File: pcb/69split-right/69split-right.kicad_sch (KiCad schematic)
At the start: 0 parts

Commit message: Figured out what GPIOs to use.
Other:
- note added: "69SPLIT RIGHT KEYBOARD"
- note added: "GPIO Outputs"
- note added: "Keyboard USB-C Connection"
- note added: "Left Keyboard"
- note added: "USB-C to PC"
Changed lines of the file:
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@@
 	(generator_version "9.0")
 	(paper "A4")
+	(arc
+		(start 103.505 97.79)
+		(mid 141.605 60.3602)
+		(end 179.705 97.79)
+		(stroke
+			(width 0)
+			(type solid)
+			(color 0 0 0 1)
+		)
+		(fill
+			(type none)
+		)
+	)
+	(rectangle
+		(start 78.74 97.79)
+		(end 130.175 152.4)
+		(stroke
+			(width 0)
+			(type default)
+		)
+		(fill
+			(type none)
+		)
+	)
+	(text "69SPLIT RIGHT KEYBOARD"
+		(exclude_from_sim no)
+		(at 143.51 36.576 0)
+		(effects
+			(font
+				(face "Book Antiqua")
+				(size 7.62 7.62)
+				(color 0 0 0 1)
+			)
+		)
+	)
+	(text "GPIO Outputs"
+		(exclude_from_sim no)
+		(at 200.025 72.644 0)
+		(effects
+			(font
+				(size 1.27 1.27)
+				(color 0 0 0 1)
+			)
+			(justify left)
+		)
+	)
+	(text "Keyboard USB-C Connection"
+		(exclude_from_sim no)
+		(at 127.635 67.31 0)
+		(effects
+			(font
+				(size 1.27 1.27)
+				(color 0 0 0 1)
+			)
+			(justify left)
+		)
+	)
+	(text "USB-C to PC"
+		(exclude_from_sim no)
+		(at 81.915 72.39 0)
+		(effects
+			(font
+				(size 1.27 1.27)
+				(color 0 0 0 1)
+			)
+			(justify left)
+		)
+	)
+	(text "Left Keyboard"
+		(exclude_from_sim no)
+		(at 102.87 123.444 0)
+		(effects
+			(font
+				(size 1.27 1.27)
+			)
+		)
+	)
+	(polyline
+		(pts
+			(xy 206.375 74.93) (xy 206.375 97.79)
+		)
+		(stroke
+			(width 0)
+			(type default)
+			(color 0 0 0 1)
+		)
+	)
+	(polyline
+		(pts
+			(xy 89.535 74.93) (xy 89.535 97.79)
+		)
+		(stroke
+			(width 0)
+			(type default)
+			(color 0 0 0 1)
+		)
+	)
+	(polyline
+		(pts
+			(xy 201.295 74.93) (xy 201.295 97.79)
+		)
+		(stroke
+			(width 0)
+			(type default)
+			(color 0 0 0 1)
+		)
+	)
+	(polyline
+		(pts
+			(xy 211.455 74.93) (xy 211.455 97.79)
+		)
+		(stroke
+			(width 0)
+			(type default)
+			(color 0 0 0 1)
+		)
+	)
+	(polyline
+		(pts
+			(xy 84.455 74.93) (xy 84.455 97.79)
+		)
+		(stroke
+			(width 0)
+			(type default)
+			(color 0 0 0 1)
+		)
+	)
 	(sheet
-		(at 111.76 72.39)
-		(size 41.91 54.61)
+		(at 156.21 97.79)
+		(size 58.42 54.61)
 		(exclude_from_sim no)
 		(in_bom yes)
@@
 		)
 		(property "Sheetname" "69split Right Keyboard"
-			(at 111.76 71.6784 0)
+			(at 156.21 97.0784 0)
 			(effects
 				(font
@@
 		)
 		(property "Sheetfile" "../right.kicad_sch"
-			(at 111.76 127.5846 0)
+			(at 156.21 152.9846 0)
 			(effects
 				(font

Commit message: I think schematic is done?
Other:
- title: (none) -> 69SPLIT KEYBOARD
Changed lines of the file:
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@@
 	(generator_version "9.0")
 	(paper "A4")
+	(title_block
+		(title "69SPLIT KEYBOARD")
+		(date "2025-06-11")
+	)
 	(arc
 		(start 103.505 97.79)

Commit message: Moved things around so it's less confusing.
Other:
- removed sheet 69split Right Keyboard
- added sheet GPIO Outputs (gpio.kicad_sch)
- added sheet Right Keyboard Connector (right-conn.kicad_sch)
- added sheet Right Matrix (right-matrix.kicad_sch)
- note added: "69SPLIT KEYBOARD"
- note added: "RIGHT SIDE"
- note removed: "69SPLIT RIGHT KEYBOARD"

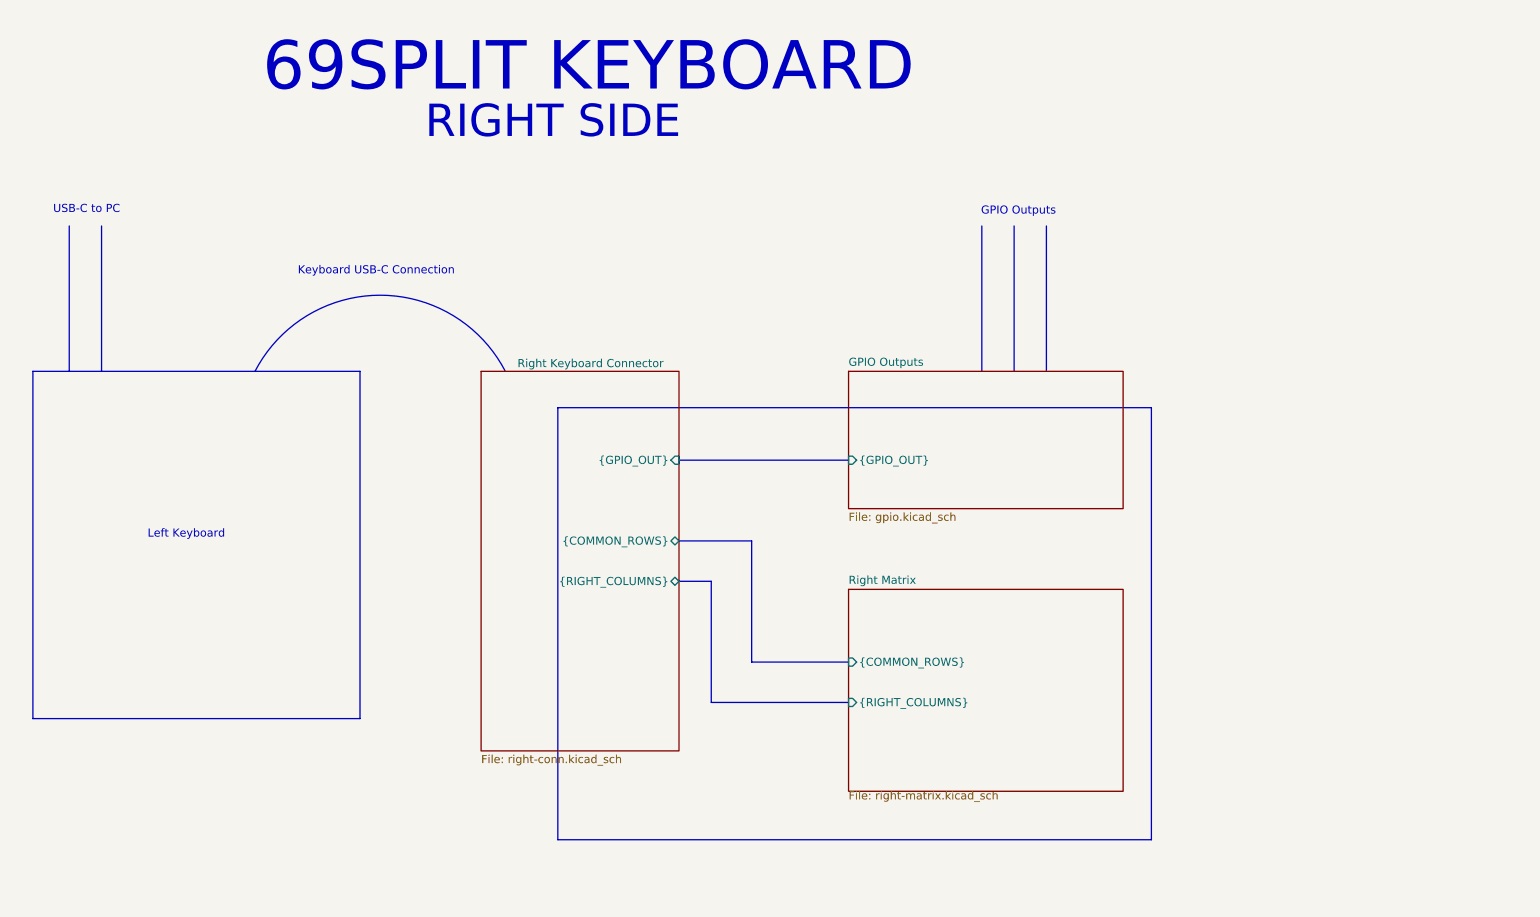
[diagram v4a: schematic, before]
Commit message: Started changing things gain to use an I/O expander with I2C.
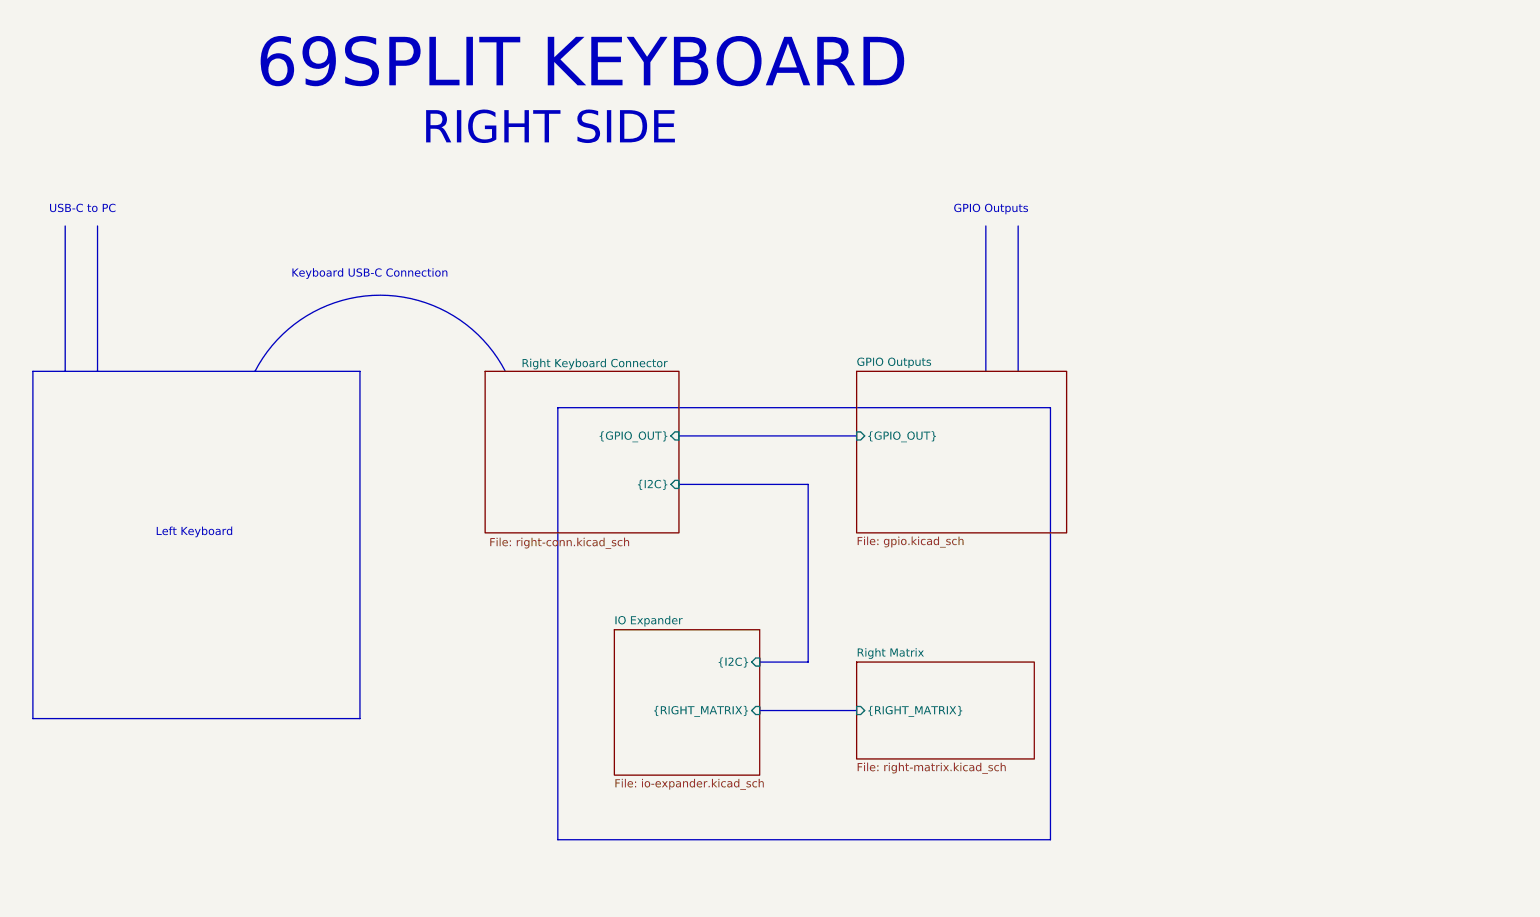
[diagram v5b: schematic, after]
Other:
- added sheet IO Expander (io-expander.kicad_sch)
- sheet Right Keyboard Connector ports: added {I2C}; removed {COMMON_ROWS}, {RIGHT_COLUMNS}
- sheet Right Matrix ports: added {RIGHT_MATRIX}; removed {COMMON_ROWS}, {RIGHT_COLUMNS}
- title: 69SPLIT KEYBOARD -> 69SPLIT
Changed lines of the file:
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@@
 	(paper "A4")
 	(title_block
-		(title "69SPLIT KEYBOARD")
-		(date "2025-06-11")
+		(title "69SPLIT")
+		(date "2025-07-28")
 		(rev "1")
 		(comment 1 "Yiannis Michael")
@@
 	(rectangle
 		(start 143.51 81.915)
-		(end 236.855 149.86)
+		(end 220.98 149.86)
 		(stroke
 			(width 0)
@@
 	(text "GPIO Outputs"
 		(exclude_from_sim no)
-		(at 210.058 51.054 0)
+		(at 205.74 50.8 0)
 		(effects
 			(font
@@
 	(text "RIGHT SIDE"
 		(exclude_from_sim no)
-		(at 142.748 37.084 0)
+		(at 142.24 38.1 0)
 		(effects
 			(font
@@
 	(text "Keyboard USB-C Connection"
 		(exclude_from_sim no)
-		(at 102.616 60.452 0)
+		(at 101.6 60.96 0)
 		(effects
 			(font
@@
 	(text "USB-C to PC"
 		(exclude_from_sim no)
-		(at 64.135 50.8 0)
+		(at 63.5 50.8 0)
 		(effects
 			(font
@@
 	(text "69SPLIT KEYBOARD"
 		(exclude_from_sim no)
-		(at 148.336 28.448 0)
+		(at 147.32 27.94 0)
 		(effects
 			(font
@@
 	(text "Left Keyboard"
 		(exclude_from_sim no)
-		(at 85.09 101.854 0)
+		(at 86.36 101.6 0)
 		(effects
 			(font
@@
 	(bus
 		(pts
-			(xy 173.99 121.92) (xy 173.99 102.87)
+			(xy 182.88 121.92) (xy 182.88 93.98)
 		)
 		(stroke
@@
 	(polyline
 		(pts
-			(xy 215.265 53.34) (xy 215.265 76.2)
+			(xy 215.9 53.34) (xy 215.9 76.2)
 		)
 		(stroke
@@
 		)
 	)
+	(polyline
+		(pts
+			(xy 71.12 53.34) (xy 71.12 76.2)
+		)
+		(stroke
+			(width 0)
+			(type default)
+			(color 0 0 0 1)
+		)
+	)
+	(polyline
+		(pts
+			(xy 210.82 53.34) (xy 210.82 76.2)
+		)
+		(stroke
+			(width 0)
+			(type default)
+			(color 0 0 0 1)
+		)
+	)
 	(bus
 		(pts
-			(xy 167.64 109.22) (xy 162.56 109.22)
+			(xy 182.88 93.98) (xy 162.56 93.98)
+		)
+		(stroke
+			(width 0)
+			(type default)
+		)
+	)
+	(bus
+		(pts
+			(xy 175.26 129.54) (xy 190.5 129.54)
+		)
+		(stroke
+			(width 0)
+			(type default)
+		)
+	)
+	(bus
+		(pts
+			(xy 162.56 86.36) (xy 190.5 86.36)
 		)
 		(stroke
@@
 	(polyline
 		(pts
-			(xy 71.755 53.34) (xy 71.755 76.2)
+			(xy 66.04 53.34) (xy 66.04 76.2)
 		)
 		(stroke
@@
 		)
 	)
-	(polyline
-		(pts
-			(xy 210.185 53.34) (xy 210.185 76.2)
-		)
-		(stroke
-			(width 0)
-			(type default)
-			(color 0 0 0 1)
-		)
-	)
 	(bus
 		(pts
-			(xy 167.64 128.27) (xy 167.64 109.22)
-		)
-		(stroke
-			(width 0)
-			(type default)
-		)
-	)
-	(polyline
-		(pts
-			(xy 220.345 53.34) (xy 220.345 76.2)
-		)
-		(stroke
-			(width 0)
-			(type default)
-			(color 0 0 0 1)
-		)
-	)
-	(bus
-		(pts
-			(xy 173.99 102.87) (xy 162.56 102.87)
-		)
-		(stroke
-			(width 0)
-			(type default)
-		)
-	)
-	(bus
-		(pts
-			(xy 167.64 128.27) (xy 189.23 128.27)
-		)
-		(stroke
-			(width 0)
-			(type default)
-		)
-	)
-	(bus
-		(pts
-			(xy 173.99 121.92) (xy 189.23 121.92)
-		)
-		(stroke
-			(width 0)
-			(type default)
-		)
-	)
-	(bus
-		(pts
-			(xy 162.56 90.17) (xy 189.23 90.17)
-		)
-		(stroke
-			(width 0)
-			(type default)
-		)
-	)
-	(polyline
-		(pts
-			(xy 66.675 53.34) (xy 66.675 76.2)
-		)
-		(stroke
-			(width 0)
-			(type default)
-			(color 0 0 0 1)
+			(xy 175.26 121.92) (xy 182.88 121.92)
+		)
+		(stroke
+			(width 0)
+			(type default)
 		)
 	)
 	(sheet
-		(at 189.23 110.49)
-		(size 43.18 31.75)
+		(at 190.5 121.92)
+		(size 27.94 15.24)
 		(exclude_from_sim no)
 		(in_bom yes)
@@
 		)
 		(property "Sheetname" "Right Matrix"
-			(at 189.23 109.7784 0)
+			(at 190.5 121.2084 0)
 			(effects
 				(font
@@
 		)
 		(property "Sheetfile" "right-matrix.kicad_sch"
-			(at 189.23 142.1896 0)
+			(at 190.5 137.7446 0)
 			(effects
 				(font
@@
 			)
 		)
-		(pin "{COMMON_ROWS}" input
-			(at 189.23 121.92 180)
-			(effects
-				(font
-					(size 1.27 1.27)
-				)
-				(justify left)
-			)
-		)
-		(pin "{RIGHT_COLUMNS}" input
-			(at 189.23 128.27 180)
+		(pin "{RIGHT_MATRIX}" input
+			(at 190.5 129.54 180)
 			(effects
 				(font
@@
 				)
 			)
+			(project ""
+				(path "/525264c0-2406-4b67-890e-0f0fc62e1056"
+					(page "#")
+				)
+			)
+			(project "69split"
+				(path "/1573ac28-80e2-4ab2-b20c-1c4896f37ece/525264c0-2406-4b67-890e-0f0fc62e1056"
+					(page "11")
+				)
+			)
 		)
 	)
 	(sheet
-		(at 131.445 76.2)
-		(size 31.115 59.69)
+		(at 152.4 116.84)
+		(size 22.86 22.86)
 		(exclude_from_sim no)
 		(in_bom yes)
 		(on_board yes)
 		(dnp no)
+		(fields_autoplaced yes)
 		(stroke
 			(width 0.1524)
@@
 			(color 0 0 0 0.0000)
 		)
+		(property "Sheetname" "IO Expander"
+			(at 152.4 116.1284 0)
+			(effects
+				(font
+					(size 1.27 1.27)
+				)
+				(justify left bottom)
+			)
+		)
+		(property "Sheetfile" "io-expander.kicad_sch"
+			(at 152.4 140.2846 0)
+			(effects
+				(font
+					(size 1.27 1.27)
+				)
+				(justify left top)
+			)
+		)
+		(pin "{I2C}" input
+			(at 175.26 121.92 0)
+			(effects
+				(font
+					(size 1.27 1.27)
+				)
+				(justify right)
+			)
+		)
+		(pin "{RIGHT_MATRIX}" input
+			(at 175.26 129.54 0)
+			(effects
+				(font
+					(size 1.27 1.27)
+				)
+				(justify right)
+			)
+		)
+		(instances
+			(project "69split-right"
+				(path "/f79c3bfa-40a7-4d04-ac4b-e56fce3d0867"
+					(page "5")
+				)
+			)
+		)
+	)
+	(sheet
+		(at 132.08 76.2)
+		(size 30.48 25.4)
+		(exclude_from_sim no)
+		(in_bom yes)
+		(on_board yes)
+		(dnp no)
+		(stroke
+			(width 0.1524)
+			(type solid)
+		)
+		(fill
+			(color 0 0 0 0.0000)
+		)
 		(property "Sheetname" "Right Keyboard Connector"
-			(at 137.16 75.692 0)
+			(at 137.795 75.692 0)
 			(effects
 				(font
@@
 		)
 		(property "Sheetfile" "right-conn.kicad_sch"
-			(at 131.445 136.4746 0)
+			(at 132.715 102.362 0)
 			(effects
 				(font
@@
 			)
 		)
-		(pin "{COMMON_ROWS}" bidirectional
-			(at 162.56 102.87 0)
+		(pin "{GPIO_OUT}" input
+			(at 162.56 86.36 0)
 			(effects
 				(font
@@
 			)
 		)
-		(pin "{RIGHT_COLUMNS}" bidirectional
-			(at 162.56 109.22 0)
-			(effects
-				(font
-					(size 1.27 1.27)
-					(thickness 0.1588)
-				)
-				(justify right)
-			)
-		)
-		(pin "{GPIO_OUT}" input
-			(at 162.56 90.17 0)
+		(pin "{I2C}" input
+			(at 162.56 93.98 0)
 			(effects
 				(font
@@
 				)
 			)
+			(project ""
+				(path "/525264c0-2406-4b67-890e-0f0fc62e1056"
+					(page "#")
+				)
+			)
+			(project "69split"
+				(path "/1573ac28-80e2-4ab2-b20c-1c4896f37ece/525264c0-2406-4b67-890e-0f0fc62e1056"
+					(page "9")
+				)
+			)
 		)
 	)
 	(sheet
-		(at 189.23 76.2)
-		(size 43.18 21.59)
+		(at 190.5 76.2)
+		(size 33.02 25.4)
 		(exclude_from_sim no)
 		(in_bom yes)
@@
 		)
 		(property "Sheetname" "GPIO Outputs"
-			(at 189.23 75.4884 0)
+			(at 190.5 75.4884 0)
 			(effects
 				(font
@@
 		)
 		(property "Sheetfile" "gpio.kicad_sch"
-			(at 189.23 98.3746 0)
+			(at 190.5 102.1846 0)
 			(effects
 				(font
@@
 		)
 		(pin "{GPIO_OUT}" input
-			(at 189.23 90.17 180)
+			(at 190.5 86.36 180)
 			(effects
 				(font
@@
 				)
 			)
-		)
-	)
-	(sheet_instances
-		(path "/"
-			(page "1")
-		)
-	)
-	(embedded_fonts no)
-	(embedded_files
-		(file
-			(name "my-sheet.kicad_wks")
-			(type worksheet)
-			(data |KLUv/WCfCS0VANadXiEQ0zb8P046AJ8aXgsH2O6IQXYrqPActbgvTGkjAgg3cCBVAFEAWAB7LP/L
-				zyw/g9G7Wic1Zntj95csGrCl1TMfak8mtWjA1HoO6fM/+QsAQEBgcj6flV5SJ+kwd6Ip+S7f25nM
-				GINlrZ1uvU6W+ty5UwAEBOfG04UeqDeFmyYieCK/t9h7g3Z+MoMOuug/ORp83WKgi71+31ftVAA8
-				WV6s4+tnaUpW8v/k/x7XCV+vGPTZIKmvv5fN7NVDMu9M7hJ8sfpv709J8jx65IM514baP+fMNtk7
-				OIwGoSb5e+MuL76z6U0o2QSbhPQWiuXnFKVZMkonUyxL8tADtUPyJ/M4lqCllL0iEm2jZJZugSk0
-				h4iAKab4XrVeFOEITC/EKOOwRZdVtgGB4bqUou7OZ4UirF9WRavlIhkEIlGAPic93r72wtU1YXvp
-				pShb6XVcXYu6cFVVWjU4bMJlWWOzrIlSECySPTSGZoBa9F674fqtaLXZg9M48TV3bYCCoOFA5pgZ
-				GklBmgxjgESExqwbzSlGCpJs4MLuYpN32QM4R7fcqQEYZYbBFb1roCZzALF1NlkveCyCWL35cxnE
-				wEKI4KJj0KsXBr6oiI1J+MtQQe+wUhcnvps4Rq/BHcNqTNlOEzNBhptObKt4AIWcYgJSlH9RNGOF
-				4k2HgwPJg0yfmc/CAzU75BLHuyCsTniNFbERpgVEeEgINsEyhIZBhCUXYQhCwScM5iHza+yObgD2
-				rqfvQX3GtNTki66yMw857Cm3qOsujTSVhoEY/SH9Q5Ui707wgLy7+D2sP38Sbw3rjn/tfXLTei5t
-				wgDnVU9KDVYzrAHGAIE4CQf8nZQ1Aw8ByJ0t3qRoW1pWI4TomR9hr1HcpCVt2Lj0DctF1FRG+kCN
-				Qa8C|
-			)
-			(checksum "4C3981DD706FE33EF3AD57A4258970D5")
-		)
-	)
+			(project ""
+				(path "/525264c0-2406-4b67-890e-0f0fc62e1056"
+					(page "#")
+				)
+			)
+			(project "69split"
+				(path "/1573ac28-80e2-4ab2-b20c-1c4896f37ece/525264c0-2406-4b67-890e-0f0fc62e1056"
+					(page "10")
+				)
+			)
+		)
+	)

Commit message: Alright I think now the left side is actually ready.
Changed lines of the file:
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@@
 	(bus
 		(pts
-			(xy 182.88 121.92) (xy 182.88 93.98)
+			(xy 180.34 121.92) (xy 180.34 93.98)
 		)
 		(stroke
@@
 	(bus
 		(pts
-			(xy 182.88 93.98) (xy 162.56 93.98)
+			(xy 180.34 93.98) (xy 162.56 93.98)
 		)
 		(stroke
@@
 	(bus
 		(pts
-			(xy 175.26 129.54) (xy 190.5 129.54)
+			(xy 175.26 134.62) (xy 190.5 134.62)
 		)
 		(stroke
@@
 	(bus
 		(pts
-			(xy 175.26 121.92) (xy 182.88 121.92)
+			(xy 175.26 121.92) (xy 180.34 121.92)
 		)
 		(stroke
@@
 	(sheet
 		(at 190.5 121.92)
-		(size 27.94 15.24)
+		(size 27.94 17.78)
 		(exclude_from_sim no)
 		(in_bom yes)
@@
 		)
 		(property "Sheetfile" "right-matrix.kicad_sch"
-			(at 190.5 137.7446 0)
+			(at 190.5 140.2846 0)
 			(effects
 				(font
@@
 		)
 		(pin "{RIGHT_MATRIX}" input
-			(at 190.5 129.54 180)
+			(at 190.5 134.62 180)
 			(effects
 				(font
@@
 		)
 		(pin "{RIGHT_MATRIX}" input
-			(at 175.26 129.54 0)
+			(at 175.26 134.62 0)
 			(effects
 				(font

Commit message: First draft of the right side.
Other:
- sheet GPIO Outputs ports: added {GPIO_EXP_OUT}; removed none
- sheet IO Expander ports: added {GPIO_EXP_OUT}; removed none
- company: (none) -> Yiannis Michael
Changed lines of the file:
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@@
 		(date "2025-07-28")
 		(rev "1")
+		(company "Yiannis Michael")
 		(comment 1 "Yiannis Michael")
 		(comment 2 "ymich9963")
@@
 		)
 	)
+	(bus
+		(pts
+			(xy 190.5 93.98) (xy 185.42 93.98)
+		)
+		(stroke
+			(width 0)
+			(type default)
+		)
+	)
 	(polyline
 		(pts
@@
 	(bus
 		(pts
+			(xy 185.42 128.27) (xy 175.26 128.27)
+		)
+		(stroke
+			(width 0)
+			(type default)
+		)
+	)
+	(bus
+		(pts
 			(xy 180.34 93.98) (xy 162.56 93.98)
 		)
@@
 		(pts
 			(xy 175.26 121.92) (xy 180.34 121.92)
+		)
+		(stroke
+			(width 0)
+			(type default)
+		)
+	)
+	(bus
+		(pts
+			(xy 185.42 93.98) (xy 185.42 128.27)
 		)
 		(stroke
@@
 			)
 		)
+		(pin "{GPIO_EXP_OUT}" input
+			(at 175.26 128.27 0)
+			(effects
+				(font
+					(size 1.27 1.27)
+				)
+				(justify right)
+			)
+		)
 		(instances
 			(project "69split-right"
@@
 			(effects
 				(font
+					(size 1.27 1.27)
+				)
+				(justify left)
+			)
+		)
+		(pin "{GPIO_EXP_OUT}" input
+			(at 190.5 93.98 180)
+			(effects
+				(font
